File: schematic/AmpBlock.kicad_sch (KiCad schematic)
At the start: 13 parts, among them IC7 LTC6090CS8E#PBF

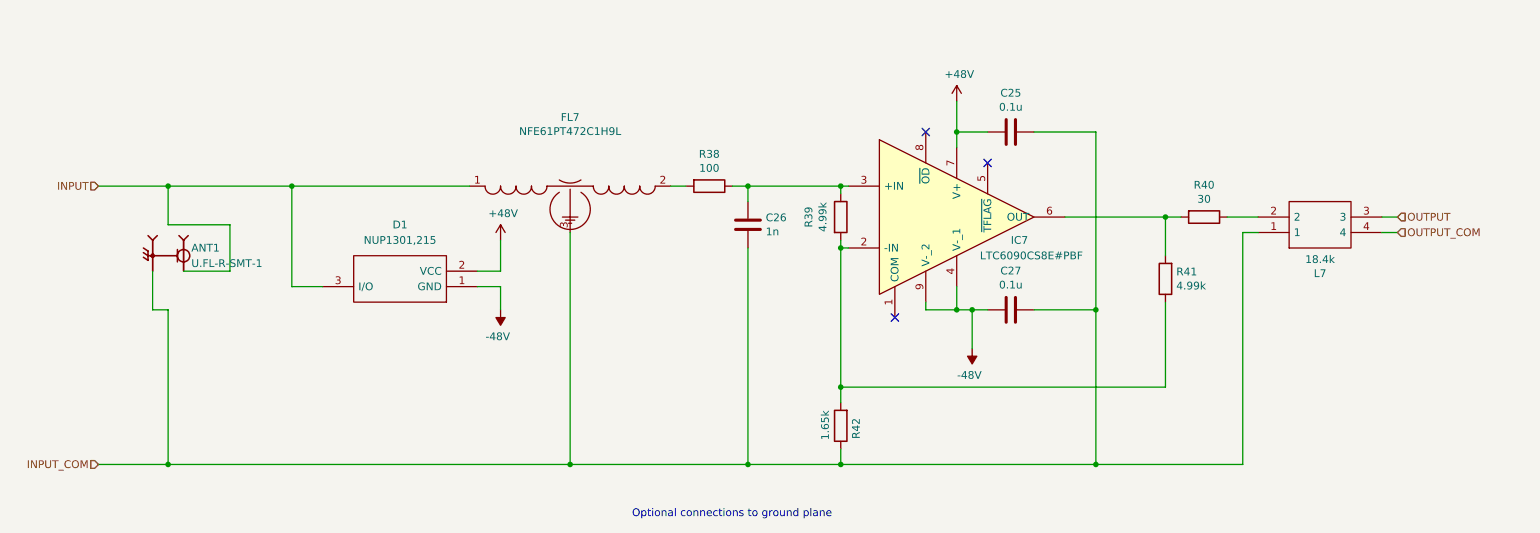
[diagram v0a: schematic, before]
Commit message: Update board design to better support enclosure with fan connect and diode connect headers. Also widen differential choke land pads and include enclosure CAD.
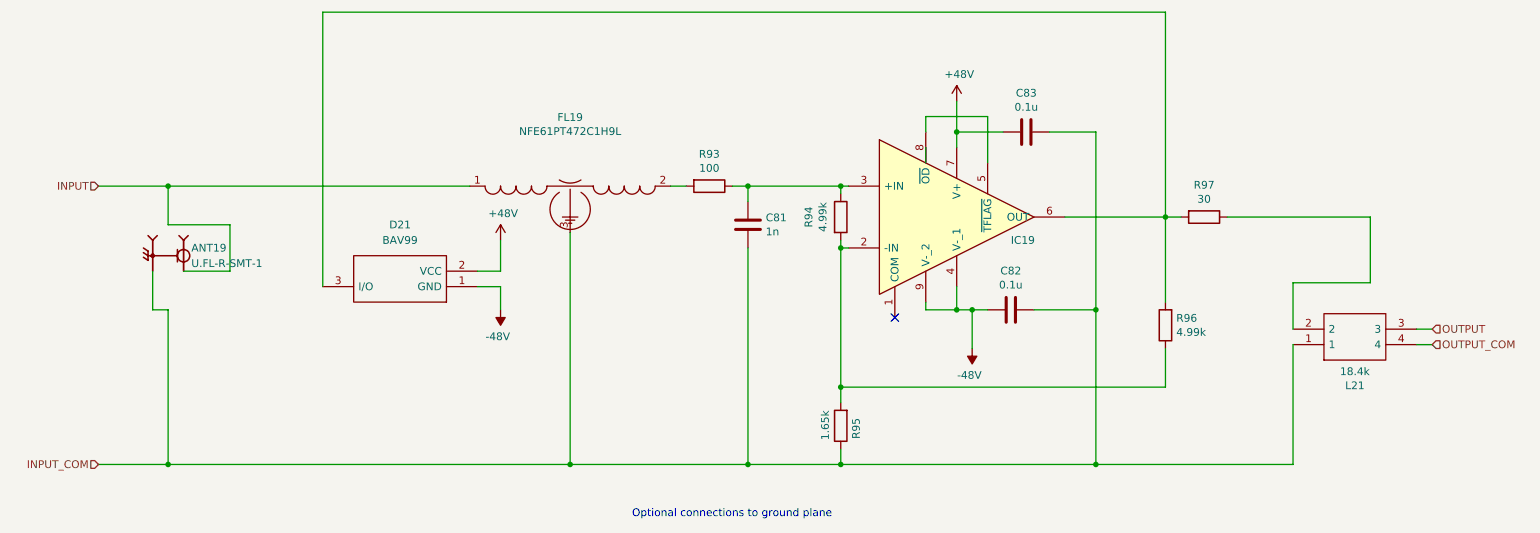
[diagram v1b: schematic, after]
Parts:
- ANT19: renamed from ANT1; AVAILABILITY Y -> (none); Availability (none) -> Y; MANUFACTURER Hirose -> (none); MPN (none) -> U.FL-R-SMT(10); Manufacturer (none) -> Hirose; Manufacturer_Part_Number U.FL-R-SMT(10) -> (none); Type (none) -> SMT
- C81: renamed from C26; AVAILABILITY Y -> (none); Availability (none) -> Y; MANUFACTURER Samsung -> (none); MPN (none) -> CL10B102KC8NNNC; Manufacturer (none) -> Samsung; Manufacturer_Part_Number CL10B102KC8NNNC -> (none); Package (none) -> 0603; Type (none) -> SMT
- C82: renamed from C27; AVAILABILITY Y -> (none); Availability (none) -> Y; MANUFACTURER Samsung -> (none); MPN (none) -> CL10B104KC8NNNC; Manufacturer (none) -> Samsung; Manufacturer_Part_Number CL10B104KC8NNNC -> (none); Package (none) -> 0603; Type (none) -> SMT
- C83: renamed from C25; AVAILABILITY Y -> (none); Availability (none) -> Y; MANUFACTURER Samsung -> (none); MPN (none) -> CL10B104KC8NNNC; Manufacturer (none) -> Samsung; Manufacturer_Part_Number CL10B104KC8NNNC -> (none)
- D21: renamed from D1; value NUP1301,215 -> BAV99; AVAILABILITY Y -> (none); Availability (none) -> Y; Digikey Number 1727-5056-2-ND -> 264-BAV99LMTR-ND; MANUFACTURER Nexperia -> (none); MPN (none) -> BAV99,LM; Manufacturer (none) -> Toshiba; Manufacturer_Part_Number NUP1301,215 -> (none); Package (none) -> SOT23; Type (none) -> SMT
- FL19: renamed from FL7; AVAILABILITY Y -> (none); Availability (none) -> Y; MANUFACTURER Murata Electronics -> (none); MPN (none) -> NFE61PT472C1H9L; Manufacturer (none) -> Murata Electronics; Manufacturer_Part_Number NFE61PT472C1H9L -> (none); Package (none) -> 2706, 3 PC Pad; Type (none) -> SMT
- IC19: renamed from IC7; value LTC6090CS8E#PBF -> (none); AVAILABILITY Y -> (none); Availability (none) -> Y; MANUFACTURER Analog Devices Inc. -> (none); MPN (none) -> LTC6090CS8E#PBF; Manufacturer (none) -> Analog Devices Inc.; Manufacturer_Part_Number LTC6090CS8E#PBF -> (none); Package (none) -> SOIC-8E; Type (none) -> SMT
- L21: renamed from L7; footprint ARTIQAmp:WE-SL2 -> ARTIQAmp:WE-SL2-WIDE; AVAILABILITY Y -> (none); Availability (none) -> Y; MANUFACTURER Wurth Elektronik -> (none); MPN (none) -> 744229; Manufacturer (none) -> Wurth Elektronik; Manufacturer_Part_Number 744229 -> (none); Type (none) -> SMT
- R93: renamed from R38; AVAILABILITY Y -> (none); Availability (none) -> Y; MANUFACTURER Stackpole Electronics Inc -> (none); MPN (none) -> RMCF0603FG100R; Manufacturer (none) -> Stackpole Electronics Inc; Manufacturer_Part_Number RMCF0603FG100R -> (none); Package (none) -> 0603; Type (none) -> SMT
- R94: renamed from R39; AVAILABILITY Y -> (none); Availability (none) -> Y; MANUFACTURER Stackpole Electronics Inc -> (none); MPN (none) -> RMCF0603FT4K99; Manufacturer (none) -> Stackpole Electronics Inc; Manufacturer_Part_Number RMCF0603FT4K99 -> (none); Package (none) -> 0603; Type (none) -> SMT
- R95: renamed from R42; AVAILABILITY Y -> (none); Availability (none) -> Y; MANUFACTURER Stackpole Electronics Inc -> (none); MPN (none) -> RMCF0603FT1K65; Manufacturer (none) -> Stackpole Electronics Inc; Manufacturer_Part_Number RMCF0603FT1K65 -> (none); Package (none) -> 0603; Type (none) -> SMT
- R96: renamed from R41; AVAILABILITY Y -> (none); Availability (none) -> Y; MANUFACTURER Stackpole Electronics Inc -> (none); MPN (none) -> RMCF0603FT4K99; Manufacturer (none) -> Stackpole Electronics Inc; Manufacturer_Part_Number RMCF0603FT4K99 -> (none); Package (none) -> 0603; Type (none) -> SMT
- R97: renamed from R40; AVAILABILITY Y -> (none); Availability (none) -> Y; MANUFACTURER Stackpole Electronics Inc -> (none); MPN (none) -> RMCF0603FT30R0; Manufacturer (none) -> Stackpole Electronics Inc; Manufacturer_Part_Number RMCF0603FT30R0 -> (none); Package (none) -> 0603; Type (none) -> SMT
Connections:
- net INPUT: no longer D21.3 (I/O)
- net at IC19.6 (OUT), R96.2, R97.2: now also D21.3 (I/O)
- net at IC19.5 (~{TFLAG}): now also IC19.8 (~{OD})
- no-connect marks 3 -> 1
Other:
- moved on the sheet: C83, L21, R96
